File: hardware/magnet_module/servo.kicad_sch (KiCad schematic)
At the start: 1 part, among them J4 Conn_01x03_Pin

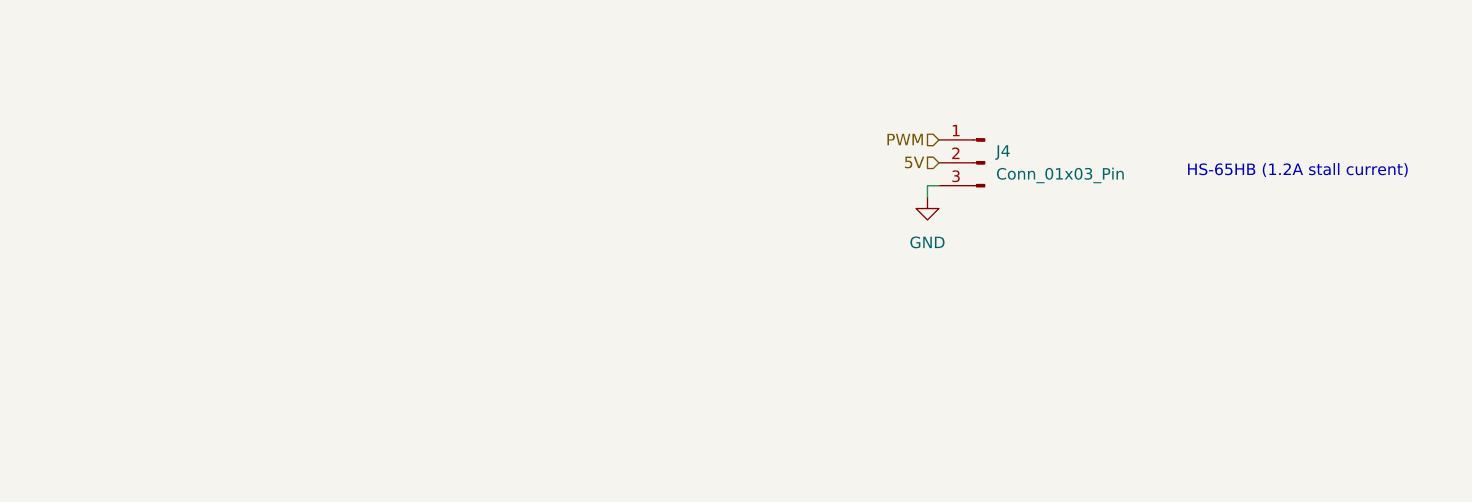
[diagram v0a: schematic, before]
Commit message: change power LED brightness, move level shifter to servo page
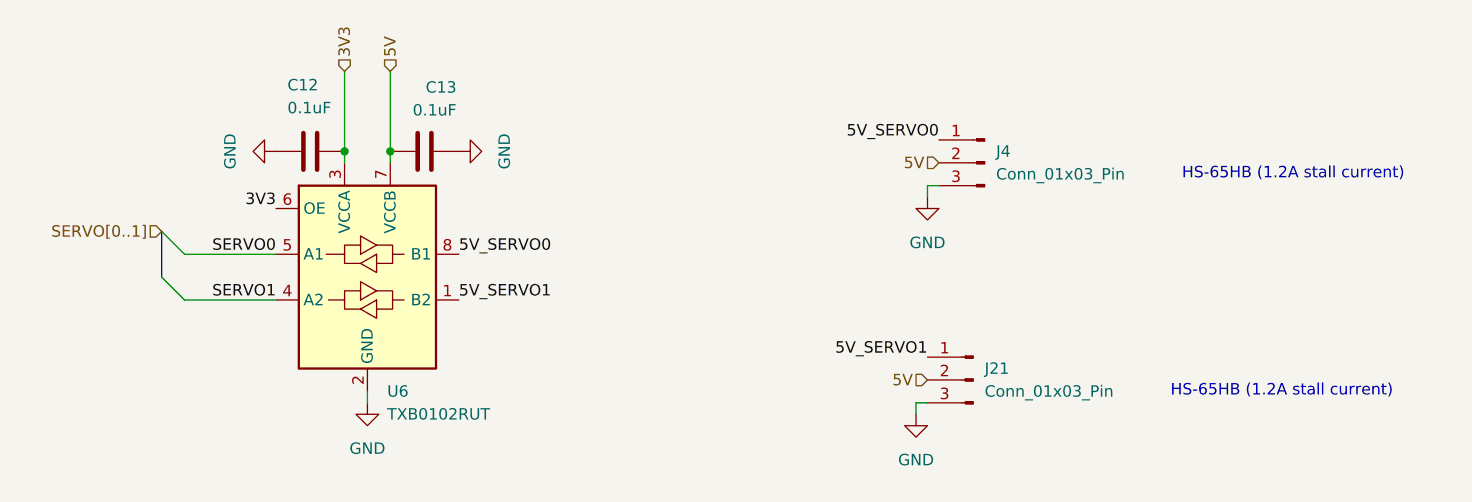
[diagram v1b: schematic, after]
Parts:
- added C12, C13: 0.1uF, symbol Device:C
- added J21: Conn_01x03_Pin, symbol Connector:Conn_01x03_Pin
- added U6: TXB0102RUT, Package_SO:TSSOP-8_3x3mm_P0.65mm, symbol Logic_LevelTranslator:TXB0102DCT
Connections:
- net 5V: now also C13.1, J21.2 (Pin_2), U6.7 (VCCB)
- net GND: now also C12.2, C13.2, J21.3 (Pin_3), U6.2 (GND)
- net PWM renamed 5V_SERVO0
- net 5V_SERVO0: now also U6.8 (B1)
- new net 3V3: C12.1, U6.3 (VCCA), U6.6 (OE)
- new net 5V_SERVO1: J21.1 (Pin_1), U6.1 (B2)
- new net SERVO0: U6.5 (A1)
- new net SERVO1: U6.4 (A2)

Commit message: add titles & esd protection for IO
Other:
- company: (none) -> Christie Lab, CU-Anschultz
- title: (none) -> Autotrainer Magnet Module - Servos
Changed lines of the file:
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@@
 	(generator_version "8.0")
 	(paper "A4")
+	(title_block
+		(title "Autotrainer Magnet Module - Servos")
+		(date "2024-07-09")
+		(rev "v1.0")
+		(company "Christie Lab, CU-Anschultz")
+		(comment 1 "Prepared by LeafLabs, LLC")
+	)
 	(junction
 		(at 68.58 97.79)

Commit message: add all PNs, relevant datasheets, and test points
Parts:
- C12, C13: footprint (none) -> Capacitor_SMD:C_0603_1608Metric; MPN (none) -> CC0603KRX7R7BB104
- U6: MPN (none) -> TXB0102RUT
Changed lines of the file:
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@@
 			)
 		)
-		(property "Footprint" ""
+		(property "Footprint" "Capacitor_SMD:C_0603_1608Metric"
 			(at 76.2 96.8248 0)
 			(effects
@@
 			)
 		)
-		(property "MPN" ""
+		(property "MPN" "CC0603KRX7R7BB104"
 			(at 72.39 97.79 0)
 			(effects
@@
 			)
 		)
-		(property "MPN" ""
+		(property "MPN" "TXB0102RUT"
 			(at 66.04 111.76 0)
 			(effects
@@
 			)
 		)
-		(property "Footprint" ""
+		(property "Footprint" "Capacitor_SMD:C_0603_1608Metric"
 			(at 55.88 96.8248 0)
 			(effects
@@
 			)
 		)
-		(property "MPN" ""
+		(property "MPN" "CC0603KRX7R7BB104"
 			(at 59.69 97.79 0)
 			(effects

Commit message: make changes as requested by Ryan
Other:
- company: Christie Lab, CU-Anschultz -> Christie Lab, CU-Anschutz
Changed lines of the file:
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@@
 		(date "2024-07-09")
 		(rev "v1.0")
-		(company "Christie Lab, CU-Anschultz")
+		(company "Christie Lab, CU-Anschutz")
 		(comment 1 "Prepared by LeafLabs, LLC")
 	)

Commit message: update PNs for BNC connectors and motor connectors
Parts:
- J21, J4: MPN B3B-XH-A -> S3B-XH-A
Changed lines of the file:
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@@
 			)
 		)
-		(property "MPN" "B3B-XH-A"
+		(property "MPN" "S3B-XH-A"
 			(at 134.62 99.06 0)
 			(effects
@@
 			)
 		)
-		(property "MPN" "B3B-XH-A"
+		(property "MPN" "S3B-XH-A"
 			(at 133.35 123.19 0)
 			(effects

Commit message: add footprints & 3d models for magnet module connector placmeent
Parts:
- J21, J4: footprint (none) -> Connector_JST:JST_XH_S3B-XH-A_1x03_P2.50mm_Horizontal
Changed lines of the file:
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@@
 			)
 		)
-		(property "Footprint" ""
+		(property "Footprint" "Connector_JST:JST_XH_S3B-XH-A_1x03_P2.50mm_Horizontal"
 			(at 134.62 99.06 0)
 			(effects
@@
 			)
 		)
-		(property "Footprint" ""
+		(property "Footprint" "Connector_JST:JST_XH_S3B-XH-A_1x03_P2.50mm_Horizontal"
 			(at 133.35 123.19 0)
 			(effects

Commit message: Tighten up the magnet module connector layout to reduce board size
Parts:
- J21, J4: footprint Connector_JST:JST_XH_S3B-XH-A_1x03_P2.50mm_Horizontal -> Connector_JST:JST_XH_B3B-XH-A_1x03_P2.50mm_Vertical
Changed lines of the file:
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@@
 			)
 		)
-		(property "Footprint" "Connector_JST:JST_XH_S3B-XH-A_1x03_P2.50mm_Horizontal"
+		(property "Footprint" "Connector_JST:JST_XH_B3B-XH-A_1x03_P2.50mm_Vertical"
 			(at 134.62 99.06 0)
 			(effects
@@
 			)
 		)
-		(property "Footprint" "Connector_JST:JST_XH_S3B-XH-A_1x03_P2.50mm_Horizontal"
+		(property "Footprint" "Connector_JST:JST_XH_B3B-XH-A_1x03_P2.50mm_Vertical"
 			(at 133.35 123.19 0)
 			(effects

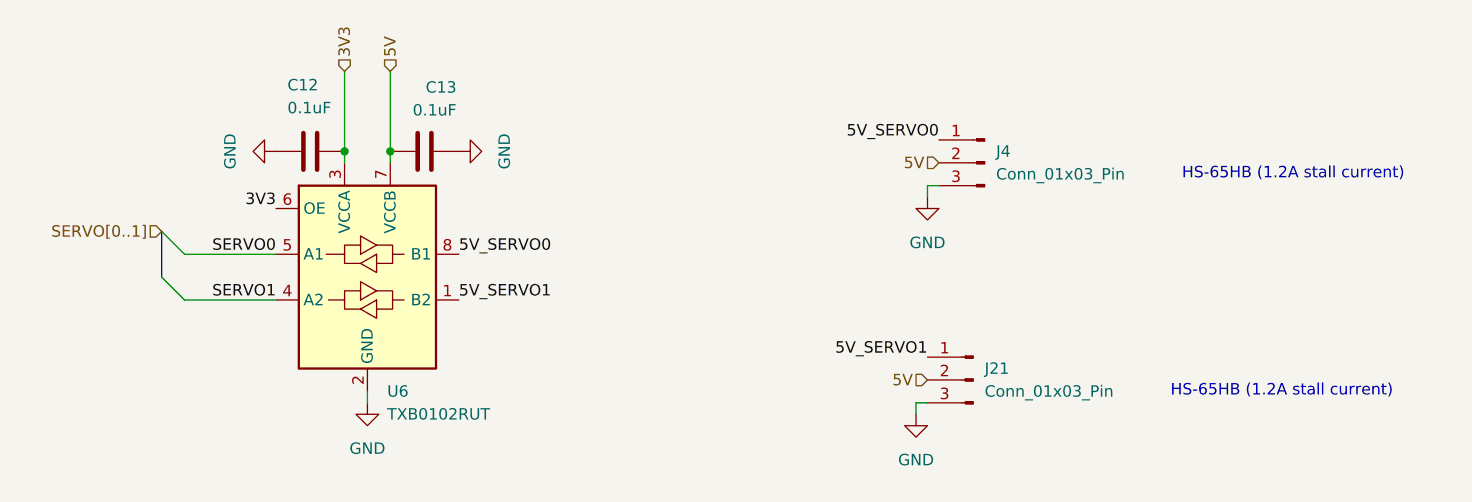
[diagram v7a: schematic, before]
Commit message: Update JST connectors MPN to reflect vertical orientation
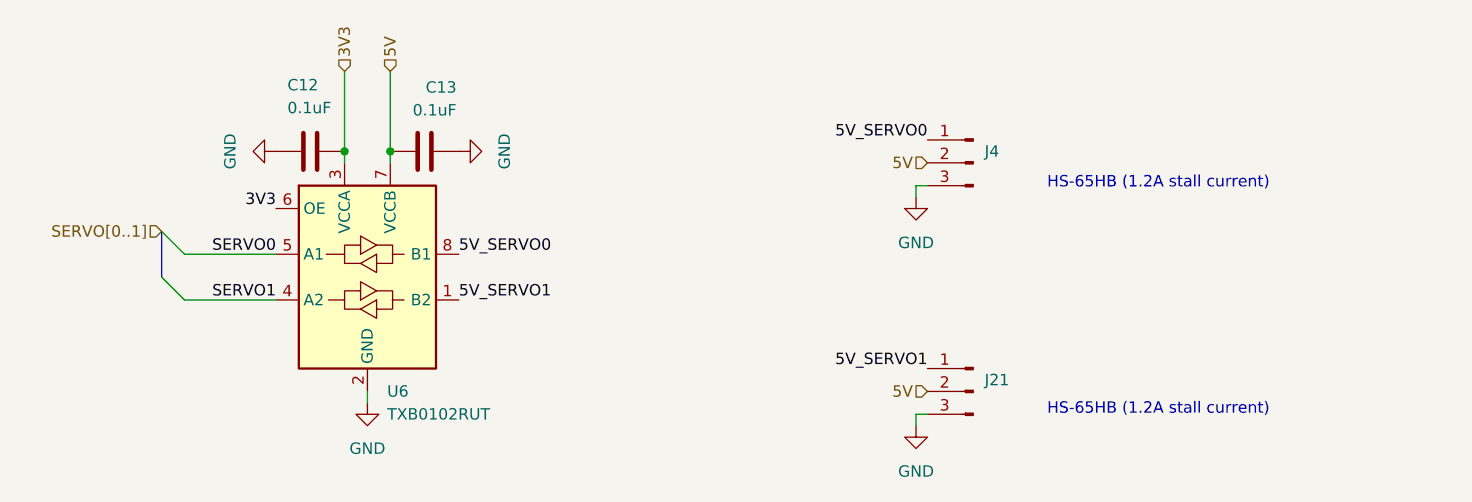
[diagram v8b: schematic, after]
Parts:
- J21, J4: MPN S3B-XH-A -> B3B-XH-A
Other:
- moved on the sheet: J21, J4
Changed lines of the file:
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@@
 	(wire
 		(pts
-			(xy 128.27 101.6) (xy 128.27 102.87)
+			(xy 127 101.6) (xy 127 102.87)
 		)
 		(stroke
@@
 	(wire
 		(pts
-			(xy 128.27 125.73) (xy 127 125.73)
+			(xy 128.27 127) (xy 127 127)
 		)
 		(stroke
@@
 	(wire
 		(pts
-			(xy 129.54 101.6) (xy 128.27 101.6)
+			(xy 128.27 101.6) (xy 127 101.6)
 		)
 		(stroke
@@
 	(wire
 		(pts
-			(xy 127 125.73) (xy 127 127)
+			(xy 127 127) (xy 127 128.27)
 		)
 		(stroke
@@
 	(text "HS-65HB (1.2A stall current)"
 		(exclude_from_sim no)
-		(at 168.91 100.33 0)
+		(at 153.924 101.346 0)
 		(effects
 			(font
@@
 	(text "HS-65HB (1.2A stall current)"
 		(exclude_from_sim no)
-		(at 167.64 124.46 0)
+		(at 153.924 126.492 0)
 		(effects
 			(font
@@
 	)
 	(label "5V_SERVO1"
-		(at 128.27 120.65 180)
+		(at 128.27 121.92 180)
 		(fields_autoplaced yes)
 		(effects
@@
 	)
 	(label "5V_SERVO0"
-		(at 129.54 96.52 180)
+		(at 128.27 96.52 180)
 		(fields_autoplaced yes)
 		(effects
@@
 	(hierarchical_label "5V"
 		(shape input)
-		(at 128.27 123.19 180)
+		(at 128.27 124.46 180)
 		(fields_autoplaced yes)
 		(effects
@@
 	(hierarchical_label "5V"
 		(shape input)
-		(at 129.54 99.06 180)
+		(at 128.27 99.06 180)
 		(fields_autoplaced yes)
 		(effects
@@
 	(symbol
 		(lib_id "power:GND")
-		(at 128.27 102.87 0)
+		(at 127 102.87 0)
 		(unit 1)
 		(exclude_from_sim no)
@@
 		(fields_autoplaced yes)
 		(property "Reference" "#PWR011"
-			(at 128.27 109.22 0)
+			(at 127 109.22 0)
 			(effects
 				(font
@@
 		)
 		(property "Value" "GND"
-			(at 128.27 107.95 0)
+			(at 127 107.95 0)
 			(effects
 				(font
@@
 		)
 		(property "Footprint" ""
-			(at 128.27 102.87 0)
+			(at 127 102.87 0)
 			(effects
 				(font
@@
 		)
 		(property "Datasheet" ""
-			(at 128.27 102.87 0)
+			(at 127 102.87 0)
 			(effects
 				(font
@@
 		)
 		(property "Description" "Power symbol creates a global label with name \"GND\" , ground"
-			(at 128.27 102.87 0)
+			(at 127 102.87 0)
 			(effects
 				(font
@@
 	(symbol
 		(lib_id "Connector:Conn_01x03_Pin")
-		(at 134.62 99.06 0)
+		(at 133.35 99.06 0)
 		(mirror y)
 		(unit 1)
@@
 		(fields_autoplaced yes)
 		(property "Reference" "J4"
-			(at 135.89 97.7899 0)
+			(at 134.62 97.7899 0)
 			(effects
 				(font
@@
 		)
 		(property "Value" "Conn_01x03_Pin"
-			(at 135.89 100.3299 0)
+			(at 134.62 100.3299 0)
 			(effects
 				(font
@@
 				)
 				(justify right)
+				(hide yes)
 			)
 		)
 		(property "Footprint" "Connector_JST:JST_XH_B3B-XH-A_1x03_P2.50mm_Vertical"
-			(at 134.62 99.06 0)
+			(at 133.35 99.06 0)
 			(effects
 				(font
@@
 		)
 		(property "Datasheet" "~"
-			(at 134.62 99.06 0)
+			(at 133.35 99.06 0)
 			(effects
 				(font
@@
 		)
 		(property "Description" "Generic connector, single row, 01x03, script generated"
-			(at 134.62 99.06 0)
-			(effects
-				(font
-					(size 1.27 1.27)
-				)
-				(hide yes)
-			)
-		)
-		(property "MPN" "S3B-XH-A"
-			(at 134.62 99.06 0)
+			(at 133.35 99.06 0)
+			(effects
+				(font
+					(size 1.27 1.27)
+				)
+				(hide yes)
+			)
+		)
+		(property "MPN" "B3B-XH-A"
+			(at 133.35 99.06 0)
 			(effects
 				(font
@@
 	(symbol
 		(lib_id "Connector:Conn_01x03_Pin")
-		(at 133.35 123.19 0)
+		(at 133.35 124.46 0)
 		(mirror y)
 		(unit 1)
@@
 		(fields_autoplaced yes)
 		(property "Reference" "J21"
-			(at 134.62 121.9199 0)
+			(at 134.62 123.1899 0)
 			(effects
 				(font
@@
 		)
 		(property "Value" "Conn_01x03_Pin"
-			(at 134.62 124.4599 0)
+			(at 134.62 125.7299 0)
 			(effects
 				(font
@@
 				)
 				(justify right)
+				(hide yes)
 			)
 		)
 		(property "Footprint" "Connector_JST:JST_XH_B3B-XH-A_1x03_P2.50mm_Vertical"
-			(at 133.35 123.19 0)
+			(at 133.35 124.46 0)
 			(effects
 				(font
@@
 		)
 		(property "Datasheet" "~"
-			(at 133.35 123.19 0)
+			(at 133.35 124.46 0)
 			(effects
 				(font
@@
 		)
 		(property "Description" "Generic connector, single row, 01x03, script generated"
-			(at 133.35 123.19 0)
-			(effects
-				(font
-					(size 1.27 1.27)
-				)
-				(hide yes)
-			)
-		)
-		(property "MPN" "S3B-XH-A"
-			(at 133.35 123.19 0)
+			(at 133.35 124.46 0)
+			(effects
+				(font
+					(size 1.27 1.27)
+				)
+				(hide yes)
+			)
+		)
+		(property "MPN" "B3B-XH-A"
+			(at 133.35 124.46 0)
 			(effects
 				(font
@@
 	(symbol
 		(lib_id "power:GND")
-		(at 127 127 0)
+		(at 127 128.27 0)
 		(unit 1)
 		(exclude_from_sim no)
@@
 		(fields_autoplaced yes)
 		(property "Reference" "#PWR079"
+			(at 127 134.62 0)
+			(effects
+				(font
+					(size 1.27 1.27)
+				)
+				(hide yes)
+			)
+		)
+		(property "Value" "GND"
 			(at 127 133.35 0)
 			(effects
@@
 					(size 1.27 1.27)
 				)
-				(hide yes)
-			)
-		)
-		(property "Value" "GND"
-			(at 127 132.08 0)
-			(effects
-				(font
-					(size 1.27 1.27)
-				)
 			)
 		)
 		(property "Footprint" ""
-			(at 127 127 0)
+			(at 127 128.27 0)
 			(effects
 				(font
@@
 		)
 		(property "Datasheet" ""
-			(at 127 127 0)
+			(at 127 128.27 0)
 			(effects
 				(font
@@
 		)
 		(property "Description" "Power symbol creates a global label with name \"GND\" , ground"
-			(at 127 127 0)
-			(effects
-				(font
+			(at 127 128.27 0)
+			(effects
+				(font
